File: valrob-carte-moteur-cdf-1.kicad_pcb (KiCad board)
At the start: 2 copper layers, 63 x 50 mm, 85 parts, among them J1 USB_C_Receptacle_USB2.0_14P, J2 Conn_01x02, J3 Conn_01x02, J4 Conn_01x04_Pin, J5 Conn_01x08, J6 Conn_01x02, J7 Conn_01x02, J8 Conn_01x08, SW1 SW_Push, SW2 SW_Push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

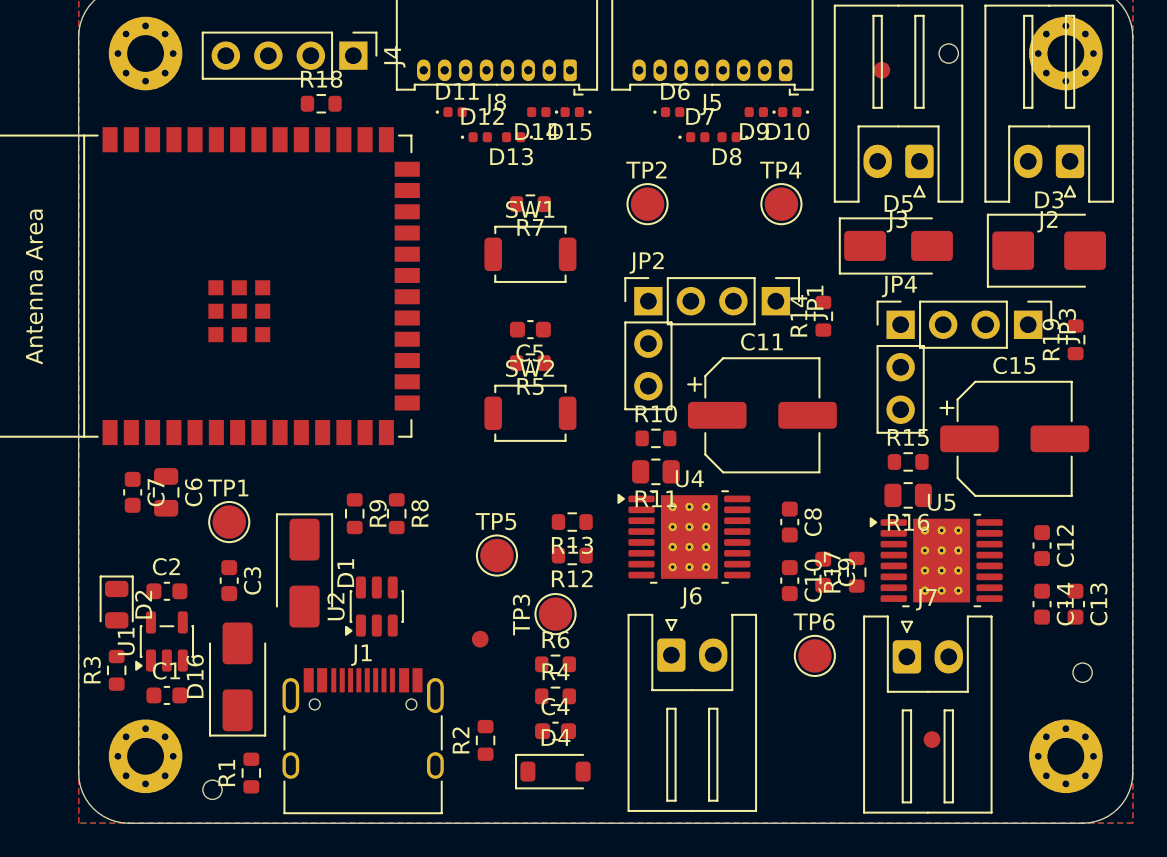
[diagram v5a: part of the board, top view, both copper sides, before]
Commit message: pcb: add ground vias
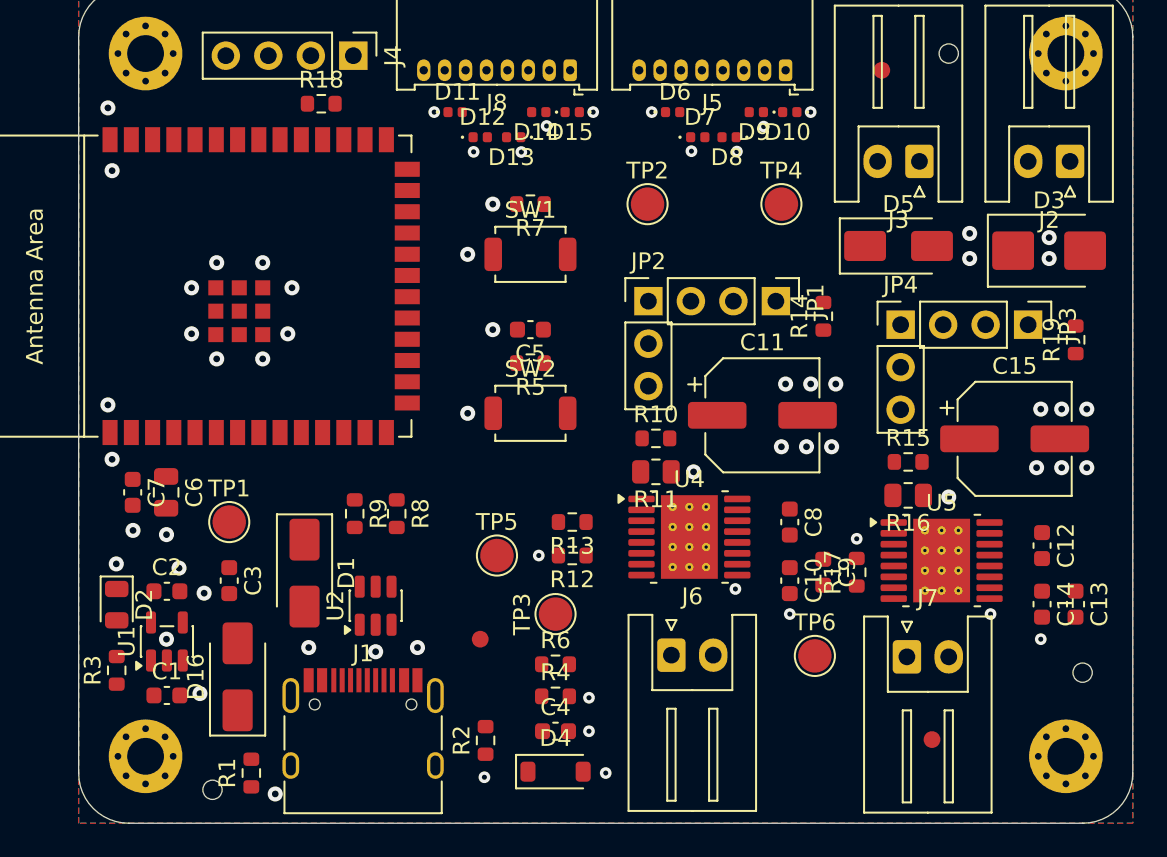
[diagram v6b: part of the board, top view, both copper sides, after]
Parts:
- moved U2 0.09 mm to (100.8, 122.0)
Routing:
- net GND: vias 0 -> 65

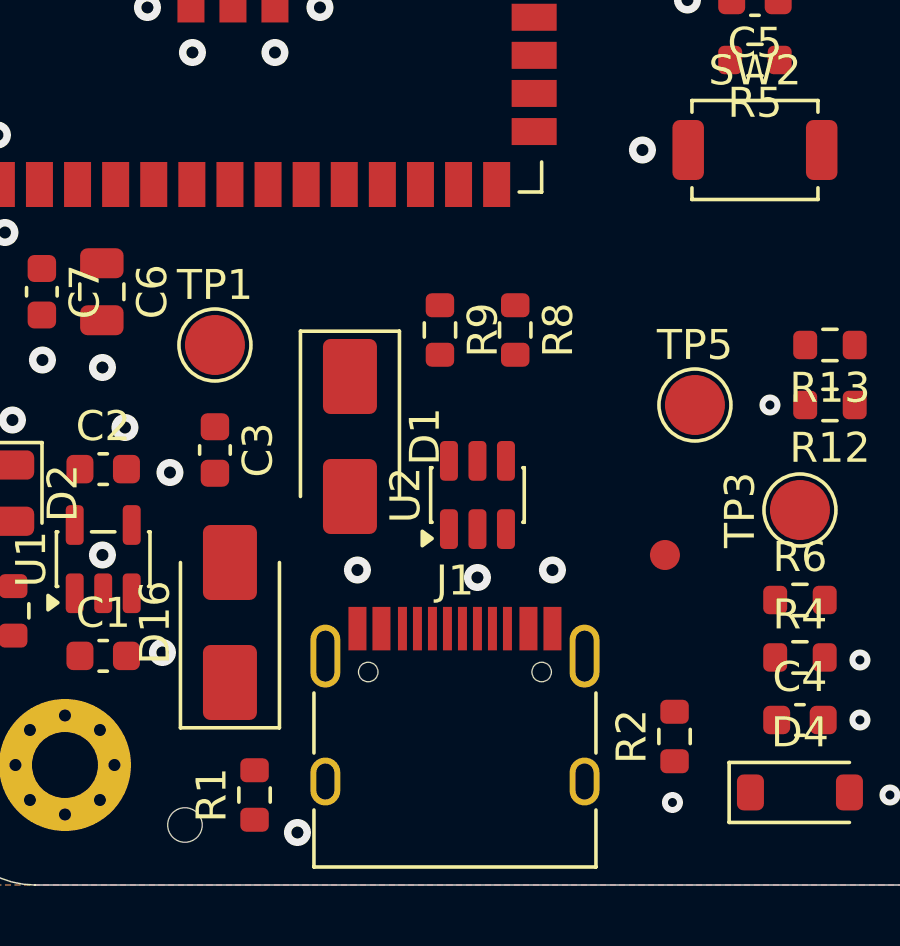
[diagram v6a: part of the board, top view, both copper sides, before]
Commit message: pcb: add usb routing
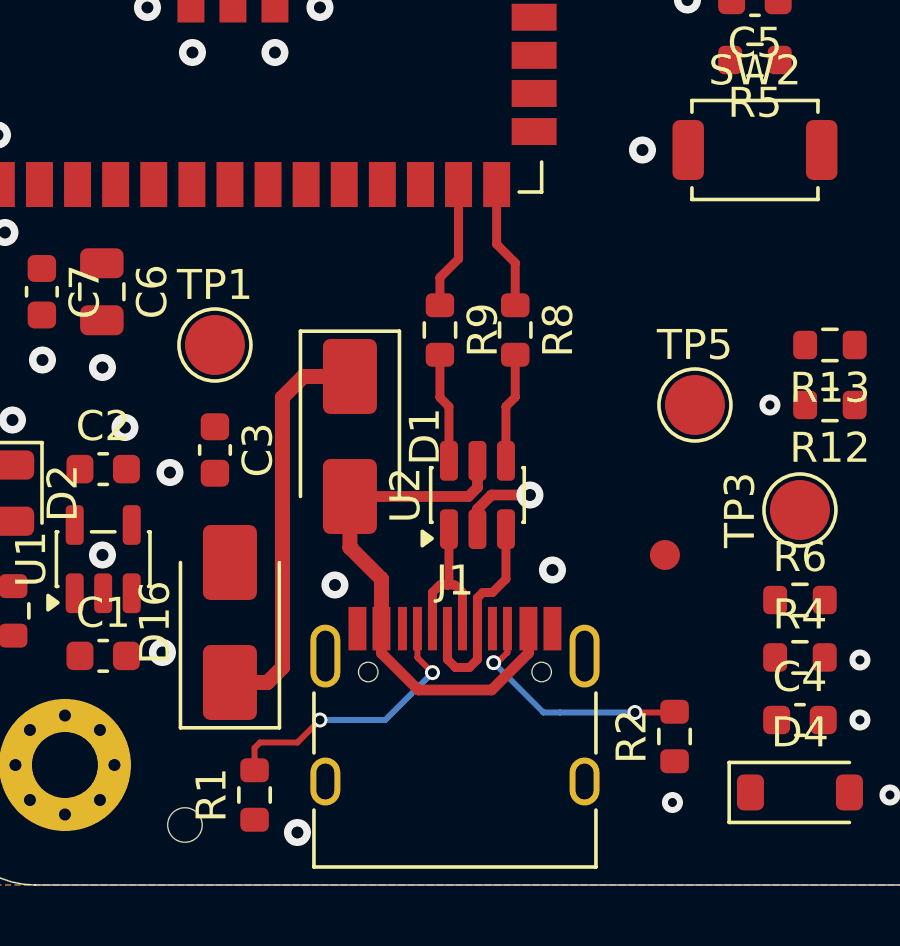
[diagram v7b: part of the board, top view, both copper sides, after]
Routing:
- net VBUS: track 0.00 -> 17.7 mm
- net +5V: track 0.00 -> 13.5 mm
- net Net-(J1-CC1): track 0.00 -> 9.39 mm, vias 0 -> 2
- net Net-(J1-CC2): track 0.00 -> 8.13 mm, vias 0 -> 2
- net Net-(J1-D+-PadA6): track 0.00 -> 7.17 mm
- net Net-(J1-D--PadA7): track 0.00 -> 5.50 mm
- net /ESP_D-: track 0.00 -> 4.28 mm
- net /ESP_D+: track 0.00 -> 4.28 mm
- net /D+: track 0.00 -> 3.67 mm
- net /D-: track 0.00 -> 3.66 mm
- net GND: track 0.00 -> 2.61 mm

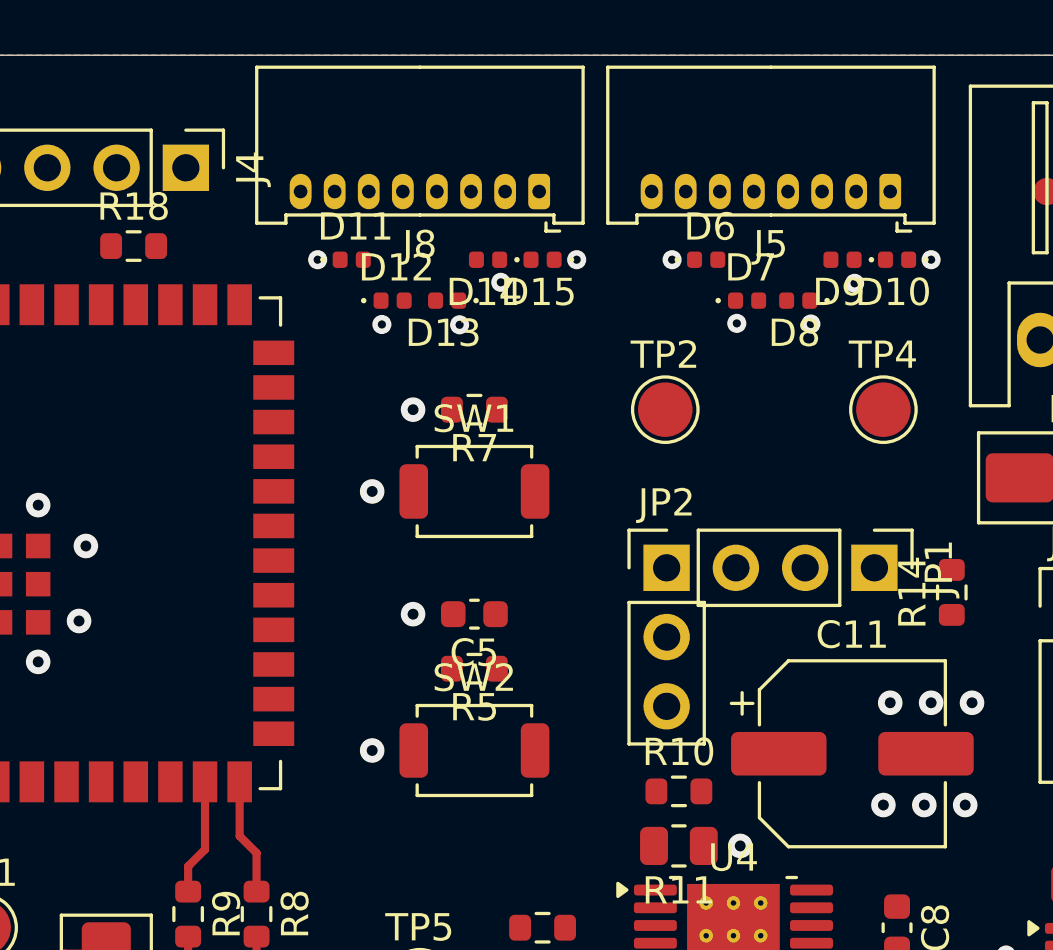
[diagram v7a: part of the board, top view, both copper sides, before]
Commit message: pcb: add SPI routing
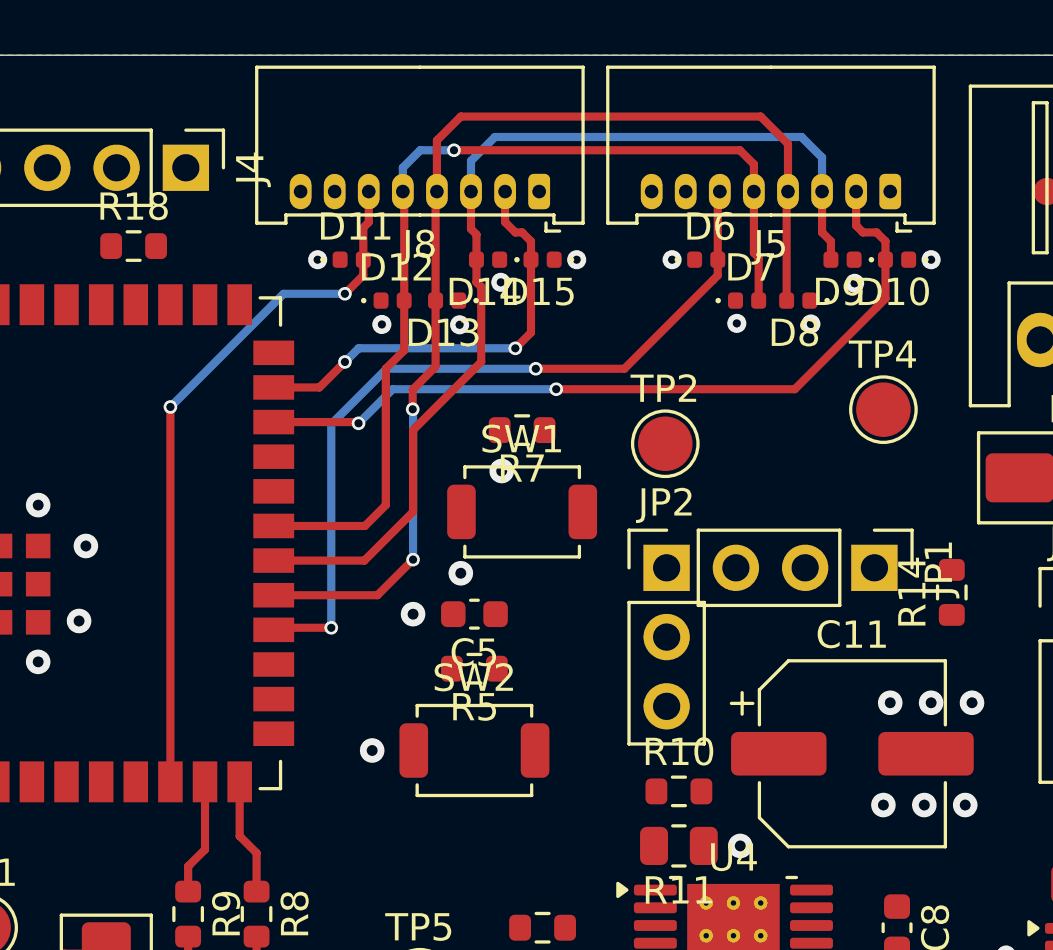
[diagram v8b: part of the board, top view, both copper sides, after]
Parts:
- moved R7 1.90 mm to (111.8, 98.8)
- moved SW1 1.90 mm to (111.8, 101.8)
- moved TP2 1.25 mm to (117.0, 99.2)
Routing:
- net /MOSI: track 0.00 -> 40.8 mm, vias 0 -> 2
- net /SCLK: track 0.00 -> 37.3 mm
- net /MISO: track 0.00 -> 35.5 mm, vias 0 -> 1
- net /CS0: track 0.00 -> 29.2 mm, vias 0 -> 2
- net /ALERT1: track 0.00 -> 29.0 mm, vias 0 -> 2
- net /CS1: track 0.00 -> 26.0 mm, vias 0 -> 2
- net /ALERT2: track 0.00 -> 16.0 mm, vias 0 -> 2
